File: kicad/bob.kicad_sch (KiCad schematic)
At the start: 39 parts

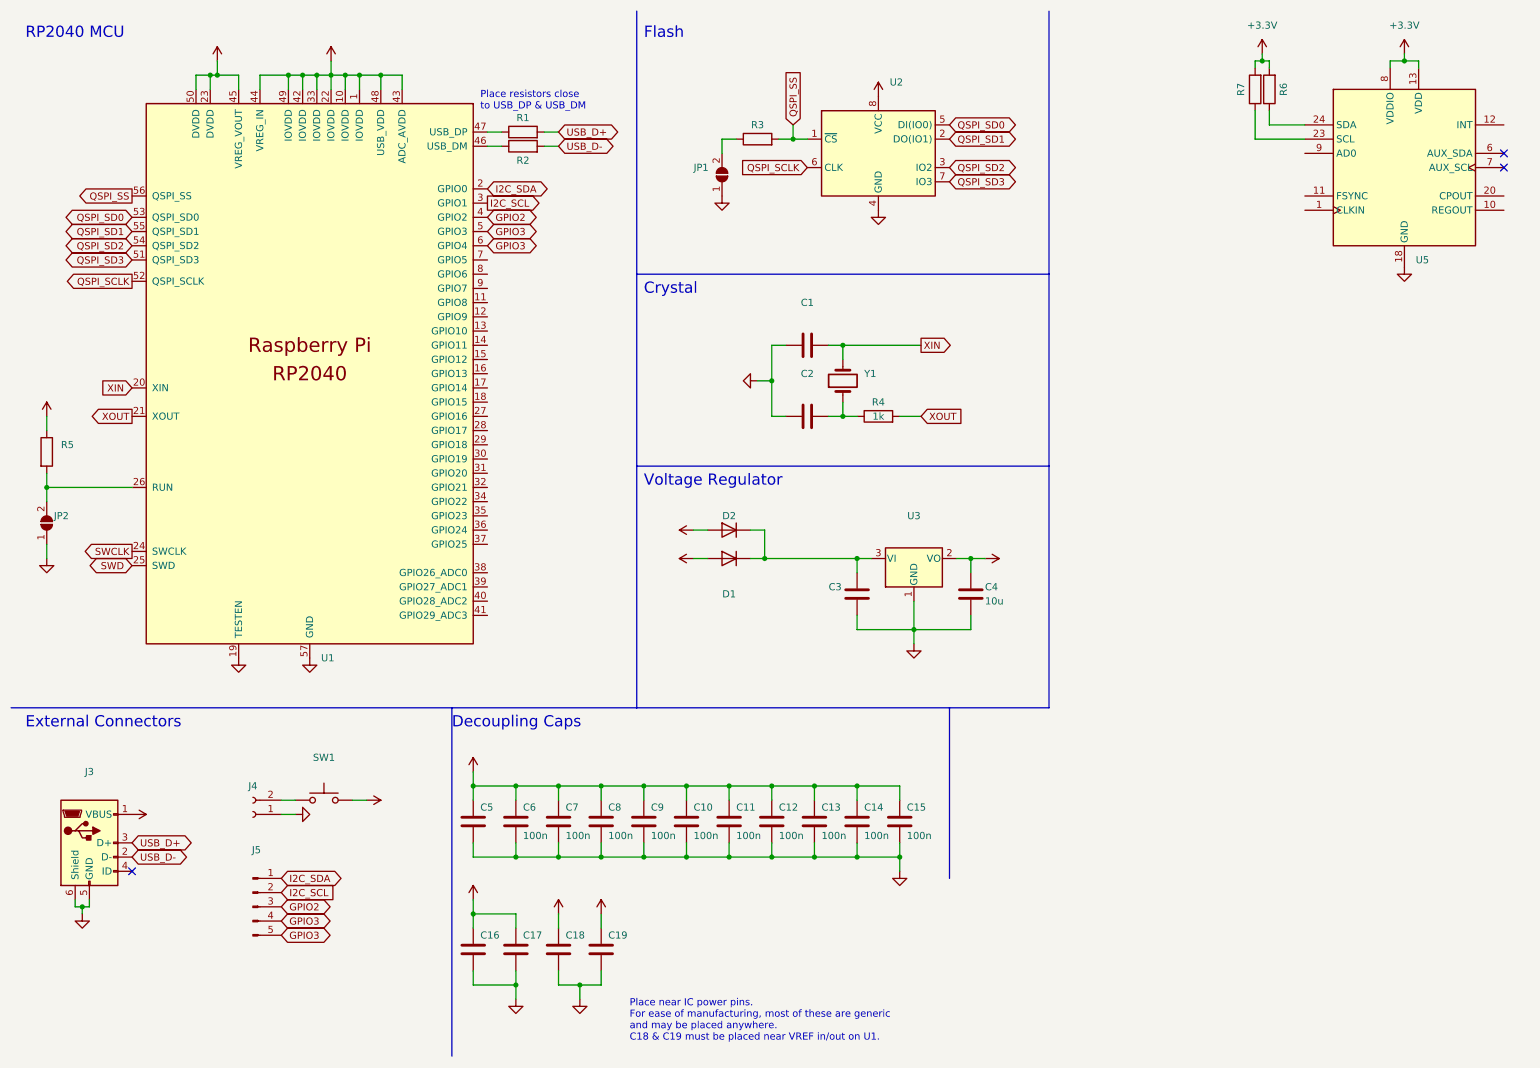
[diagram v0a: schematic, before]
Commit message: Rearranged directories
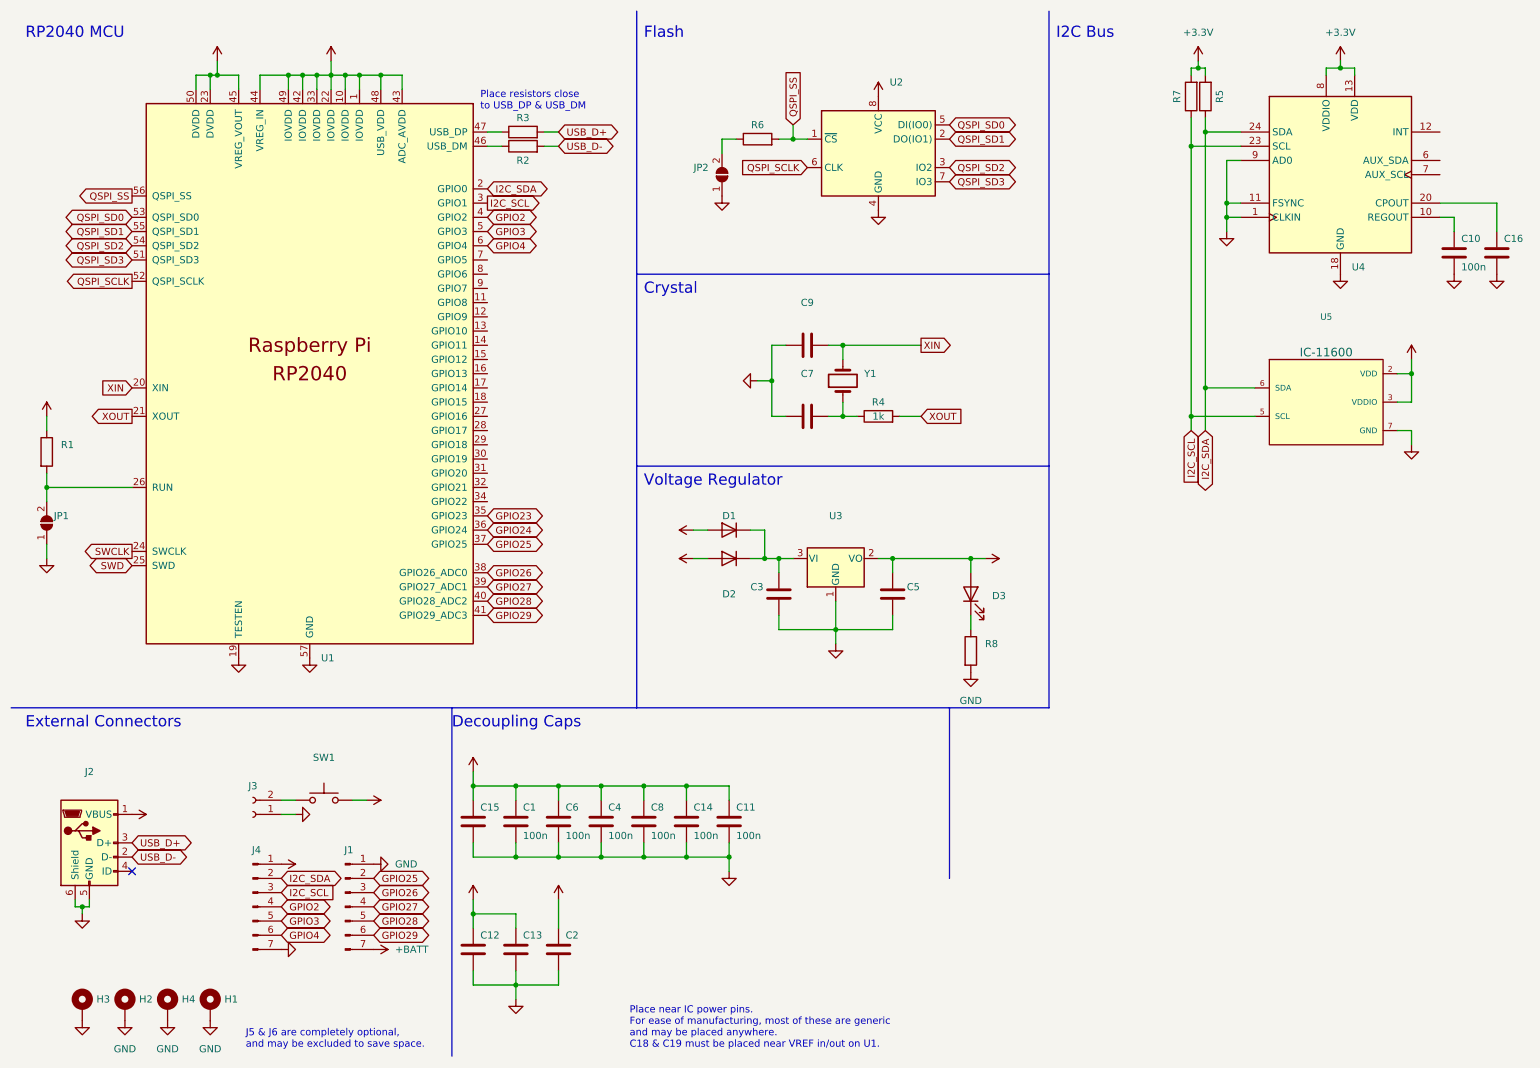
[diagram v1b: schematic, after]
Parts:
- removed C13, C15, C7: 100n, Capacitor_SMD:C_0402_1005Metric, symbol Device:C
- removed C17: (no value), symbol Device:C
- added C16: (no value), Capacitor_SMD:C_0402_1005Metric, symbol Device:C
- added D3: (no value), symbol Device:LED
- added H1, H2, H4: MountingHole_Pad, MountingHole:MountingHole_2.2mm_M2_DIN965_Pad, symbol Mechanical:MountingHole_Pad
- added H3: (no value), symbol Mechanical:MountingHole_Pad
- added J1: GPIO (Optional), Connector_PinHeader_2.54mm:PinHeader_1x07_P2.54mm_Vertical, symbol Connector:Conn_01x07_Male
- added R8: (no value), symbol Device:R
- added U5: (no value), symbol SparkFun-Sensors:BMP180
- C5: renamed from C4; value 10u -> (none)
- J4: renamed from J5; symbol Connector:Conn_01x05_Male -> Connector:Conn_01x07_Male
- renumbered C6 to C1, C14 to C11, C16 to C12, C18 to C13, C12 to C14, C5 to C15, C19 to C2, C9 to C4, C8 to C6, C2 to C7, C11 to C8, C1 to C9, D2 to D1, D1 to D2, J3 to J2, J4 to J3, JP2 to JP1, JP1 to JP2, R5 to R1, R1 to R3, R6 to R5, R3 to R6, U5 to U4
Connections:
- net +3V3: now also J4.1 (Pin_1), D3.2 (A), U5.2 (VDD), U5.3 (VDDIO); no longer C10.1
- net +BATT: now also J1.7 (Pin_7)
- net GND: now also J4.7 (Pin_7), U4.1 (CLKIN), U4.11 (FSYNC), U4.9 (AD0), C16.2, H1.1, H2.1, H3.1, H4.1, J1.1 (Pin_1), R8.2, U5.7 (GND)
- net GPIO2: now also J4.4 (Pin_4); no longer J4.3 (Pin_3)
- net GPIO3: no longer J4.4 (Pin_4), U1.6 (GPIO4)
- net I2C_SCL: now also J4.3 (Pin_3), R7.1, U4.23 (SCL), U5.5 (SCL); no longer J4.2 (Pin_2)
- net I2C_SDA: now also J4.2 (Pin_2), R5.1, U4.24 (SDA), U5.6 (SDA); no longer J4.1 (Pin_1)
- net at U4.10 (REGOUT): now also C10.1
- net at U4.20 (CPOUT): now also C16.1
- net GPIO23: now reaches U1.35 (GPIO23)
- net GPIO24: now reaches U1.36 (GPIO24)
- net GPIO25: now reaches U1.37 (GPIO25)
- net GPIO25: now also J1.2 (Pin_2)
- net GPIO26: now reaches U1.38 (GPIO26_ADC0)
- net GPIO26: now also J1.3 (Pin_3)
- net GPIO27: now reaches U1.39 (GPIO27_ADC1)
- net GPIO27: now also J1.4 (Pin_4)
- net GPIO28: now reaches U1.40 (GPIO28_ADC2)
- net GPIO28: now also J1.5 (Pin_5)
- net GPIO29: now reaches U1.41 (GPIO29_ADC3)
- net GPIO29: now also J1.6 (Pin_6)
- new net: D3.1 (K), R8.1
- new net GPIO4: J4.6 (Pin_6), U1.6 (GPIO4)
- no-connect marks 3 -> 1
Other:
- note added: "I2C Bus"
- note added: "J5 & J6 are completely optional, and may be excluded to save space."
- moved on the sheet: C11, C13, C14, C2, C3, C4, C5, C6, C8, R5, R7, U3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

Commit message: Fixed MPU6050 charge pump cap
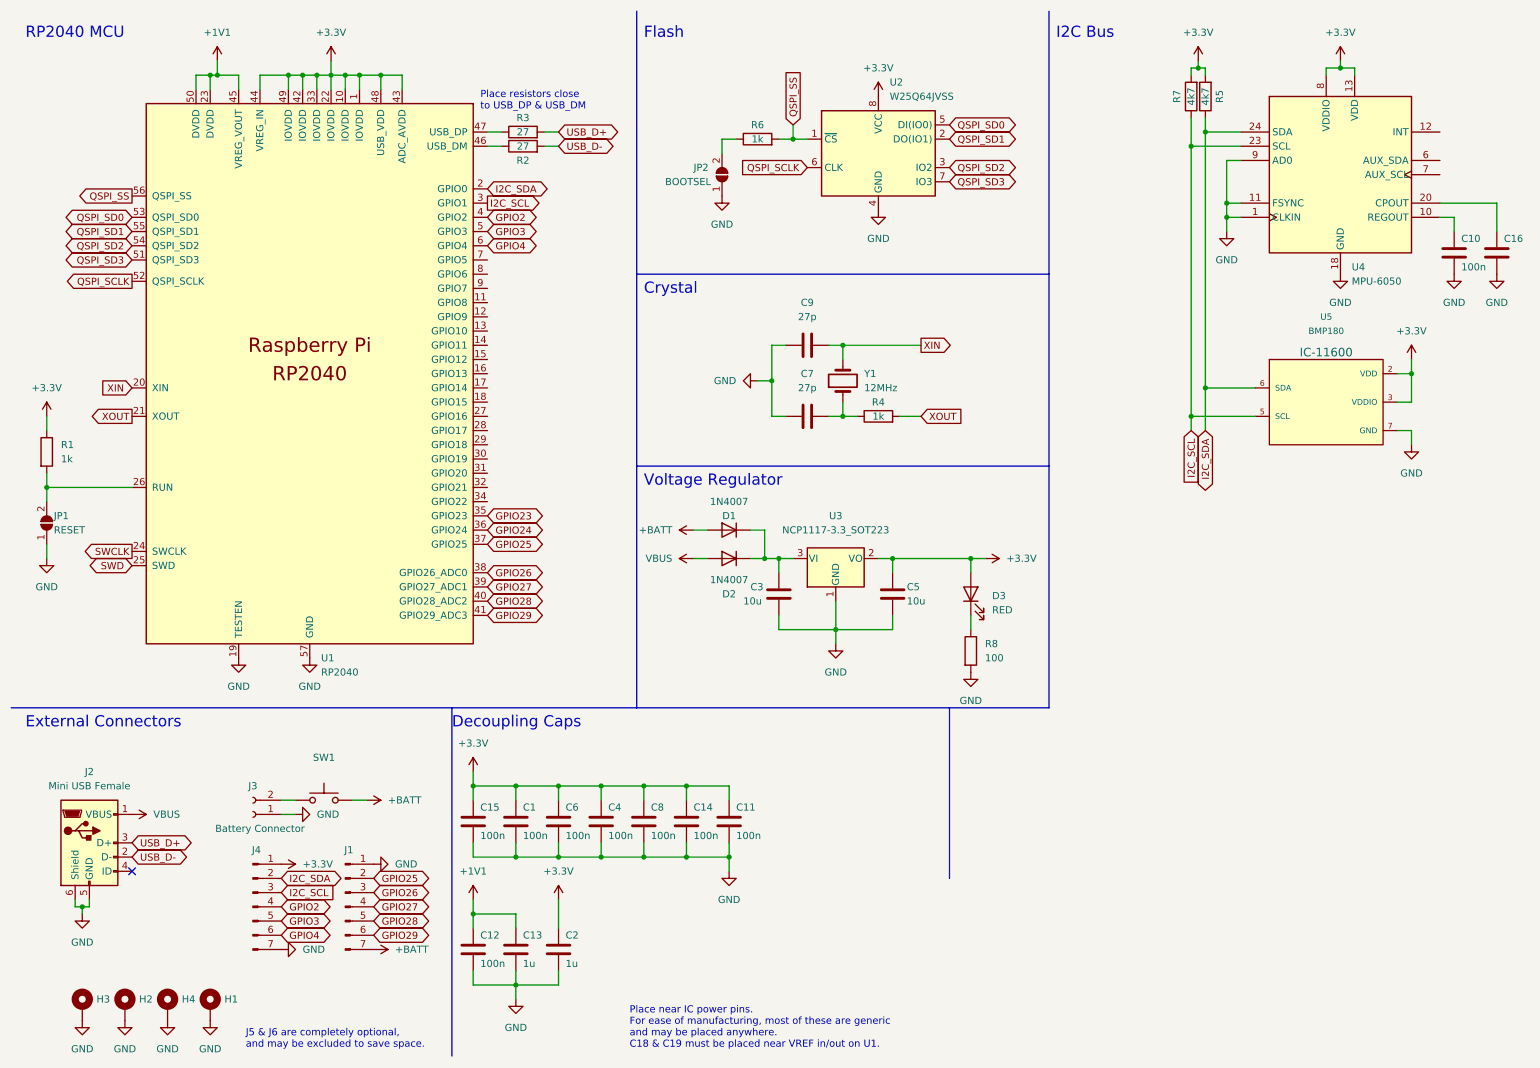
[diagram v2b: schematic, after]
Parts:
- C12, C15: value (none) -> 100n; footprint (none) -> Capacitor_SMD:C_0402_1005Metric
- C13, C2: value (none) -> 1u
- C16: footprint Capacitor_SMD:C_0402_1005Metric -> (none)
- C3, C5: value (none) -> 10u; footprint (none) -> Capacitor_SMD:C_0603_1608Metric
- C7, C9: value (none) -> 27p; footprint (none) -> Capacitor_SMD:C_0402_1005Metric
- D1, D2: value (none) -> 1N4007; footprint (none) -> Diode_SMD:D_SOD-123
- D3: value (none) -> RED; footprint (none) -> LED_THT:LED_D3.0mm
- H3: value (none) -> MountingHole_Pad; footprint (none) -> MountingHole:MountingHole_2.2mm_M2_DIN965_Pad
- J2: value (none) -> Mini USB Female; footprint (none) -> Connector_USB:USB_Mini-B_Lumberg_2486_01_Horizontal
- J3: value (none) -> Battery Connector; footprint (none) -> Connector_Wire:Compact_Relief
- J4: value (none) -> GPIO (Optional); footprint (none) -> Connector_PinHeader_2.54mm:PinHeader_1x07_P2.54mm_Vertical
- JP1: value (none) -> RESET
- JP2: value (none) -> BOOTSEL; footprint (none) -> Jumper:SolderJumper-2_P1.3mm_Open_TrianglePad1.0x1.5mm
- R1: value (none) -> 1k; footprint (none) -> Resistor_SMD:R_0402_1005Metric
- R2: value (none) -> 27
- R3: value (none) -> 27; footprint (none) -> Resistor_SMD:R_0402_1005Metric
- R5, R7: value (none) -> 4k7
- R6: value (none) -> 1k
- R8: value (none) -> 100; footprint (none) -> Resistor_SMD:R_0402_1005Metric
- SW1: value (none) -> Screw Switch; footprint (none) -> Connector:Screw_Switch_M3
- U1: value (none) -> RP2040; footprint (none) -> RP2040_minimal:RP2040-QFN-56
- U2: value (none) -> W25Q64JVSS; footprint (none) -> Package_SO:SOIC-8_5.23x5.23mm_P1.27mm
- U3: value (none) -> NCP1117-3.3_SOT223; footprint (none) -> Package_TO_SOT_SMD:SOT-223-3_TabPin2
- U4: value (none) -> MPU-6050; footprint (none) -> Sensor_Motion:InvenSense_QFN-24_4x4mm_P0.5mm
- U5: value (none) -> BMP180; footprint (none) -> Silicon-Custom:BMP180
- Y1: value (none) -> 12MHz; footprint (none) -> Crystal:Crystal_SMD_5032-2Pin_5.0x3.2mm

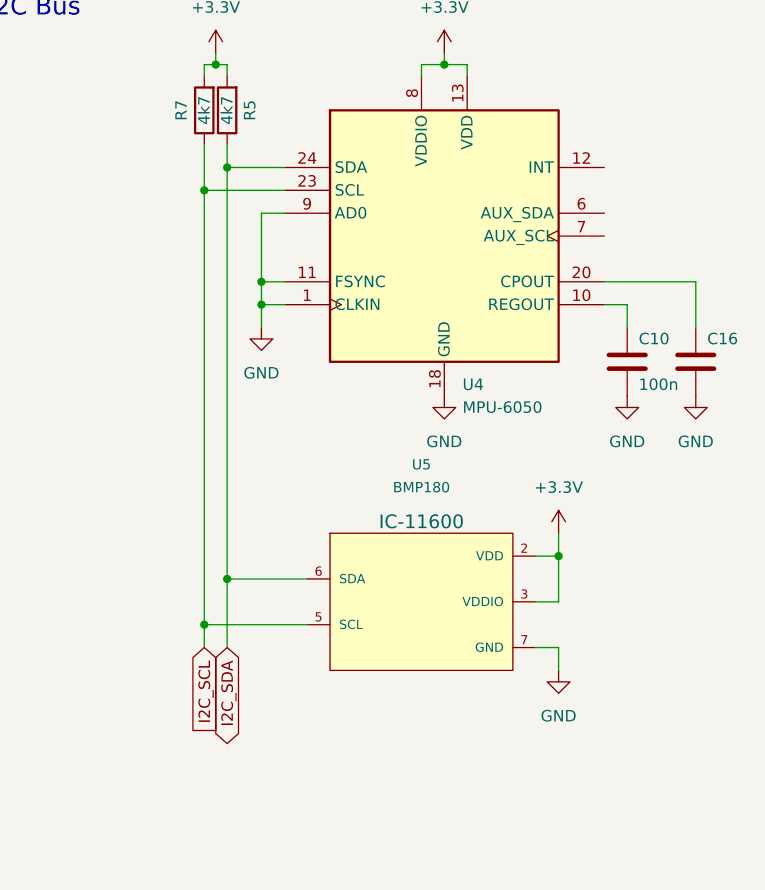
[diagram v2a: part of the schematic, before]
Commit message: Replaced BMP180 with HP203B
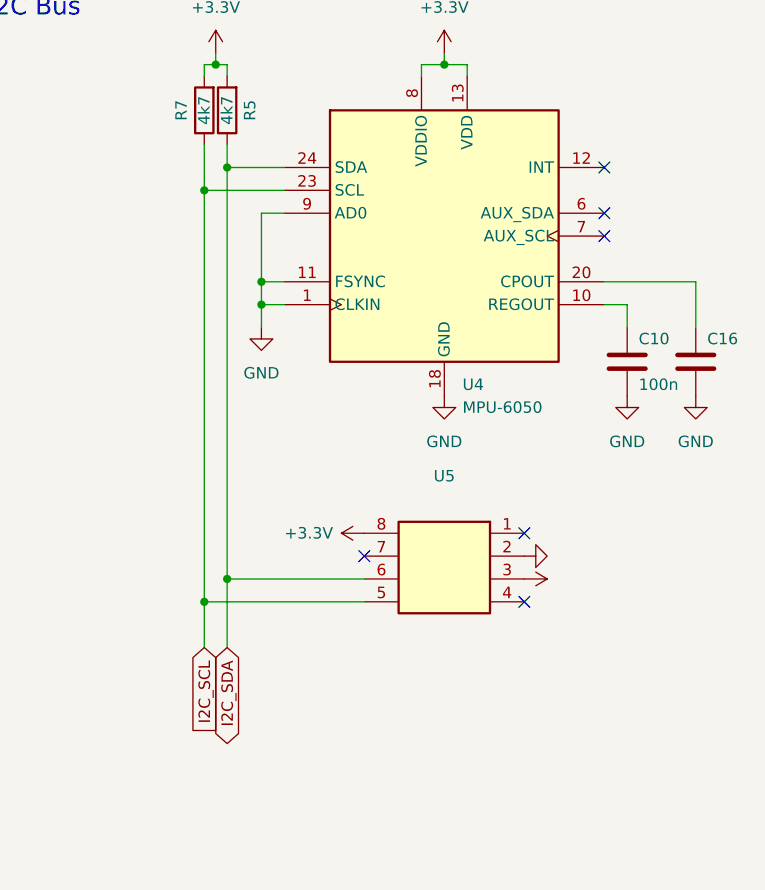
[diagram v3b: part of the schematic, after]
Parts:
- removed U5: BMP180, Silicon-Custom:BMP180, symbol SparkFun-Sensors:BMP180
- added U5: (no value), symbol IC_Generic:IC8
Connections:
- net +3V3: now also U5.3, U5.8
- net GND: now also U5.2
- net I2C_SCL: now also U5.5
- net I2C_SDA: now also U5.6
- no-connect marks 1 -> 7

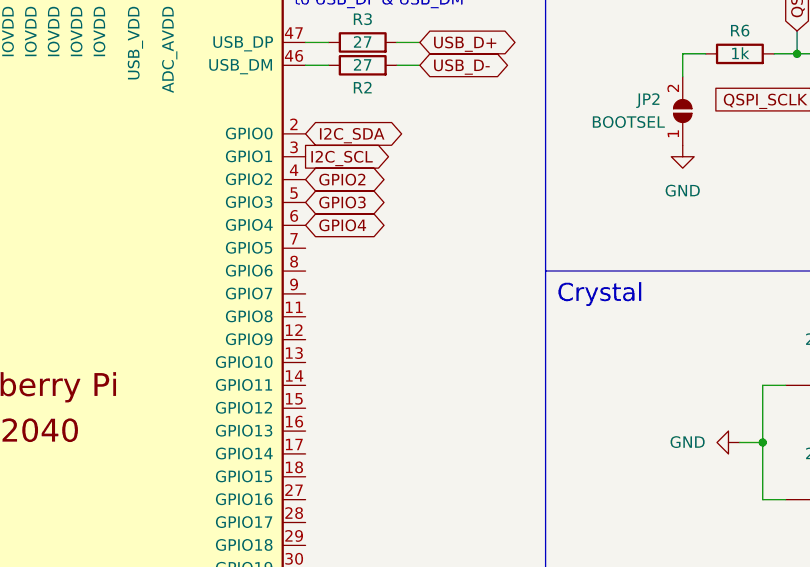
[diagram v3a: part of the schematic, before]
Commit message: Added piezo buzzer
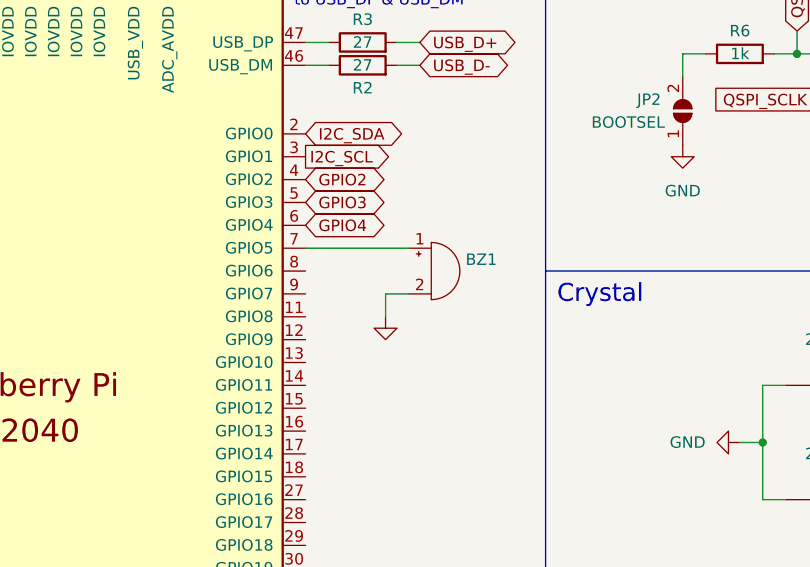
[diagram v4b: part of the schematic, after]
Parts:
- added BZ1: (no value), symbol Device:Buzzer
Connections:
- net GND: now also BZ1.2 (+)
- net at U1.7 (GPIO5): now also BZ1.1 (-)
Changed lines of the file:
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@@
+    (stroke (width 0) (type default) (color 0 0 0 0))
+  )
+  (wire (pts (xy 104.14 60.96) (xy 104.14 63.5))
     (stroke (width 0) (type default) (color 0 0 0 0))
   )
@@
     (stroke (width 0) (type default) (color 0 0 0 0))
   )
+  (wire (pts (xy 106.68 60.96) (xy 104.14 60.96))
+    (stroke (width 0) (type default) (color 0 0 0 0))
+  )
   (wire (pts (xy 130.81 149.86) (xy 130.81 152.4))
     (stroke (width 0) (type default) (color 0 0 0 0))
@@
   )
   (polyline (pts (xy 195.58 135.89) (xy 195.58 92.71))
+    (stroke (width 0) (type default) (color 0 0 0 0))
+  )
+  (wire (pts (xy 95.25 55.88) (xy 106.68 55.88))
     (stroke (width 0) (type default) (color 0 0 0 0))
   )
@@
     (pin "2")
   )
+  (symbol (lib_id "Device:Buzzer") (at 109.22 58.42 0) (unit 1)
+    (in_bom yes) (on_board yes) (fields_autoplaced)
+    (property "Reference" "BZ1" (id 0) (at 113.03 57.1499 0)
+      (effects (font (size 1.27 1.27)) (justify left))
+    )
+    (property "Value" "" (id 1) (at 113.03 59.6899 0)
+      (effects (font (size 1.27 1.27)) (justify left))
+    )
+    (property "Footprint" "" (id 2) (at 108.585 55.88 90)
+      (effects (font (size 1.27 1.27)) hide)
+    )
+    (property "Datasheet" "~" (id 3) (at 108.585 55.88 90)
+      (effects (font (size 1.27 1.27)) hide)
+    )
+    (pin "1")
+    (pin "2")
+  )
   (symbol (lib_id "power:+1V1") (at 46.99 20.32 0) (unit 1)
     (in_bom yes) (on_board yes) (fields_autoplaced)
@@
     (pin "1")
     (pin "2")
+  )
+  (symbol (lib_id "power:GND") (at 104.14 63.5 0) (unit 1)
+    (in_bom yes) (on_board yes) (fields_autoplaced)
+    (property "Reference" "#PWR?" (id 0) (at 104.14 69.85 0)
+      (effects (font (size 1.27 1.27)) hide)
+    )
+    (property "Value" "" (id 1) (at 104.14 68.58 0))
+    (property "Footprint" "" (id 2) (at 104.14 63.5 0)
+      (effects (font (size 1.27 1.27)) hide)
+    )
+    (property "Datasheet" "" (id 3) (at 104.14 63.5 0)
+      (effects (font (size 1.27 1.27)) hide)
+    )
+    (pin "1")
   )
   (symbol (lib_id "Device:R") (at 16.51 90.17 0) (unit 1)
@@
       (reference "#PWR0140") (unit 1) (value "GND") (footprint "")
     )
+    (path "/16cdadb5-6329-4729-9c41-af8600d7857b"
+      (reference "#PWR?") (unit 1) (value "GND") (footprint "")
+    )
     (path "/9e8dc75f-ed3e-4f69-95dc-da579f1b179f"
       (reference "#PWR?") (unit 1) (value "+3.3V") (footprint "")
@@
       (reference "#PWR?") (unit 1) (value "GND") (footprint "")
     )
+    (path "/0c0afd09-1d3f-47c4-bdfb-8409bb16aa71"
+      (reference "BZ1") (unit 1) (value "Buzzer") (footprint "Buzzer_Beeper:Buzzer_12x9.5RM7.6")
+    )
     (path "/00b942de-1e62-476c-a78f-85d1dc0d5dee"
